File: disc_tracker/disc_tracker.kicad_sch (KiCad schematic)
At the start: 0 parts

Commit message: QFN32 added for Silabs chip. Regulator symbol added. All ICs on schematic
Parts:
- added AE1: Antenna_Chip, RF_Antenna:Pulse_W3011, symbol Device:Antenna_Chip
- added IC1: EFR32BG22C112F352GM32-CR, Package_DFN_QFN:QFN-32-1EP_4x4mm_P0.4mm_EP2.8x2.8mm, symbol RF_Bluetooth:EFR32BG22C112F352GM32-CR
- added J1: Conn_01x02_Pin, Connector_JST:JST_PH_B2B-PH-K_1x02_P2.00mm_Vertical, symbol Connector:Conn_01x02_Pin
- added U1: AP9101CK6, Package_TO_SOT_SMD:SOT-23-6, symbol Battery_Management:AP9101CK6
- added U2: TCR2LF33, Package_TO_SOT_SMD:SOT-553, symbol Regulator_Linear:TCR2LF33
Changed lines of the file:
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@@
 (kicad_sch (version 20230121) (generator eeschema)
   (paper "A4")
+  (symbol (lib_id "Battery_Management:AP9101CK6") (at 59.69 49.53 0) (unit 1)
+    (in_bom yes) (on_board yes) (dnp no) (fields_autoplaced)
+    (property "Reference" "U1" (at 61.8841 39.37 0)
+      (effects (font (size 1.27 1.27)) (justify left))
+    )
+    (property "Value" "AP9101CK6" (at 61.8841 41.91 0)
+      (effects (font (size 1.27 1.27)) (justify left))
+    )
+    (property "Footprint" "Package_TO_SOT_SMD:SOT-23-6" (at 59.69 49.53 0)
+      (effects (font (size 1.27 1.27)) hide)
+    )
+    (property "Datasheet" "https://www.diodes.com/assets/Datasheets/AP9101C.pdf" (at 59.69 48.26 0)
+      (effects (font (size 1.27 1.27)) hide)
+    )
+    (pin "1")
+    (pin "2")
+    (pin "3")
+    (pin "4")
+    (pin "5")
+    (pin "6")
+    (instances
+      (project "disc_tracker"
+        (path "/50d77920-ac47-47b2-845c-3d52e036b015"
+          (reference "U1") (unit 1)
+        )
+      )
+    )
+  )
+  (symbol (lib_id "Connector:Conn_01x02_Pin") (at 35.56 31.75 0) (unit 1)
+    (in_bom yes) (on_board yes) (dnp no) (fields_autoplaced)
+    (property "Reference" "J1" (at 36.195 26.67 0)
+      (effects (font (size 1.27 1.27)))
+    )
+    (property "Value" "Conn_01x02_Pin" (at 36.195 29.21 0)
+      (effects (font (size 1.27 1.27)))
+    )
+    (property "Footprint" "Connector_JST:JST_PH_B2B-PH-K_1x02_P2.00mm_Vertical" (at 35.56 31.75 0)
+      (effects (font (size 1.27 1.27)) hide)
+    )
+    (property "Datasheet" "~" (at 35.56 31.75 0)
+      (effects (font (size 1.27 1.27)) hide)
+    )
+    (pin "1")
+    (pin "2")
+    (instances
+      (project "disc_tracker"
+        (path "/50d77920-ac47-47b2-845c-3d52e036b015"
+          (reference "J1") (unit 1)
+        )
+      )
+    )
+  )
+  (symbol (lib_id "RF_Bluetooth:EFR32BG22C112F352GM32-CR") (at 120.65 76.2 0) (unit 1)
+    (in_bom yes) (on_board yes) (dnp no) (fields_autoplaced)
+    (property "Reference" "IC1" (at 172.72 69.2719 0)
+      (effects (font (size 1.27 1.27)))
+    )
+    (property "Value" "EFR32BG22C112F352GM32-CR" (at 172.72 71.8119 0)
+      (effects (font (size 1.27 1.27)))
+    )
+    (property "Footprint" "Package_DFN_QFN:QFN-32-1EP_4x4mm_P0.4mm_EP2.8x2.8mm" (at 157.48 158.42 0)
+      (effects (font (size 1.27 1.27)) (justify left top) hide)
+    )
+    (property "Datasheet" "https://au.mouser.com/datasheet/2/368/efr32bg22c112_datasheet-1830161.pdf" (at 157.48 258.42 0)
+      (effects (font (size 1.27 1.27)) (justify left top) hide)
+    )
+    (property "Height" "0.9" (at 157.48 458.42 0)
+      (effects (font (size 1.27 1.27)) (justify left top) hide)
+    )
+    (property "Mouser Part Number" "634-ER32BG22112352CR" (at 157.48 558.42 0)
+      (effects (font (size 1.27 1.27)) (justify left top) hide)
+    )
+    (property "Mouser Price/Stock" "https://www.mouser.co.uk/ProductDetail/Silicon-Labs/EFR32BG22C112F352GM32-CR?qs=zhx2xqPtQQy3D8%2FKsJy7oA%3D%3D" (at 157.48 658.42 0)
+      (effects (font (size 1.27 1.27)) (justify left top) hide)
+    )
+    (property "Manufacturer_Name" "Silicon Labs" (at 157.48 758.42 0)
+      (effects (font (size 1.27 1.27)) (justify left top) hide)
+    )
+    (property "Manufacturer_Part_Number" "EFR32BG22C112F352GM32-CR" (at 157.48 858.42 0)
+      (effects (font (size 1.27 1.27)) (justify left top) hide)
+    )
+    (pin "1")
+    (pin "10")
+    (pin "11")
+    (pin "12")
+    (pin "13")
+    (pin "14")
+    (pin "15")
+    (pin "16")
+    (pin "17")
+    (pin "18")
+    (pin "19")
+    (pin "2")
+    (pin "20")
+    (pin "21")
+    (pin "22")
+    (pin "23")
+    (pin "24")
+    (pin "25")
+    (pin "26")
+    (pin "27")
+    (pin "28")
+    (pin "29")
+    (pin "3")
+    (pin "30")
+    (pin "31")
+    (pin "32")
+    (pin "33")
+    (pin "4")
+    (pin "5")
+    (pin "6")
+    (pin "7")
+    (pin "8")
+    (pin "9")
+    (instances
+      (project "disc_tracker"
+        (path "/50d77920-ac47-47b2-845c-3d52e036b015"
+          (reference "IC1") (unit 1)
+        )
+      )
+    )
+  )
+  (symbol (lib_id "Device:Antenna_Chip") (at 254 33.02 0) (unit 1)
+    (in_bom yes) (on_board yes) (dnp no) (fields_autoplaced)
+    (property "Reference" "AE1" (at 259.08 29.21 0)
+      (effects (font (size 1.27 1.27)) (justify left))
+    )
+    (property "Value" "Antenna_Chip" (at 259.08 31.75 0)
+      (effects (font (size 1.27 1.27)) (justify left))
+    )
+    (property "Footprint" "RF_Antenna:Pulse_W3011" (at 251.46 28.575 0)
+      (effects (font (size 1.27 1.27)) hide)
+    )
+    (property "Datasheet" "~" (at 251.46 28.575 0)
+      (effects (font (size 1.27 1.27)) hide)
+    )
+    (pin "1")
+    (pin "2")
+    (instances
+      (project "disc_tracker"
+        (path "/50d77920-ac47-47b2-845c-3d52e036b015"
+          (reference "AE1") (unit 1)
+        )
+      )
+    )
+  )
+  (symbol (lib_id "Regulator_Linear:TCR2LF33") (at 107.95 36.83 0) (unit 1)
+    (in_bom yes) (on_board yes) (dnp no) (fields_autoplaced)
+    (property "Reference" "U2" (at 107.95 26.67 0)
+      (effects (font (size 1.27 1.27)))
+    )
+    (property "Value" "TCR2LF33" (at 107.95 29.21 0)
+      (effects (font (size 1.27 1.27)))
+    )
+    (property "Footprint" "Package_TO_SOT_SMD:SOT-553" (at 107.95 46.99 0)
+      (effects (font (size 1.27 1.27)) hide)
+    )
+    (property "Datasheet" "https://au.mouser.com/datasheet/2/408/TCR2LF10_datasheet_en_20141106-760799.pdf" (at 101.6 30.48 0)
+      (effects (font (size 1.27 1.27)) hide)
+    )
+    (pin "1")
+    (pin "2")
+    (pin "3")
+    (pin "4")
+    (pin "5")
+    (instances
+      (project "disc_tracker"
+        (path "/50d77920-ac47-47b2-845c-3d52e036b015"
+          (reference "U2") (unit 1)
+        )
+      )
+    )
+  )
   (sheet_instances
     (path "/" (page "1"))

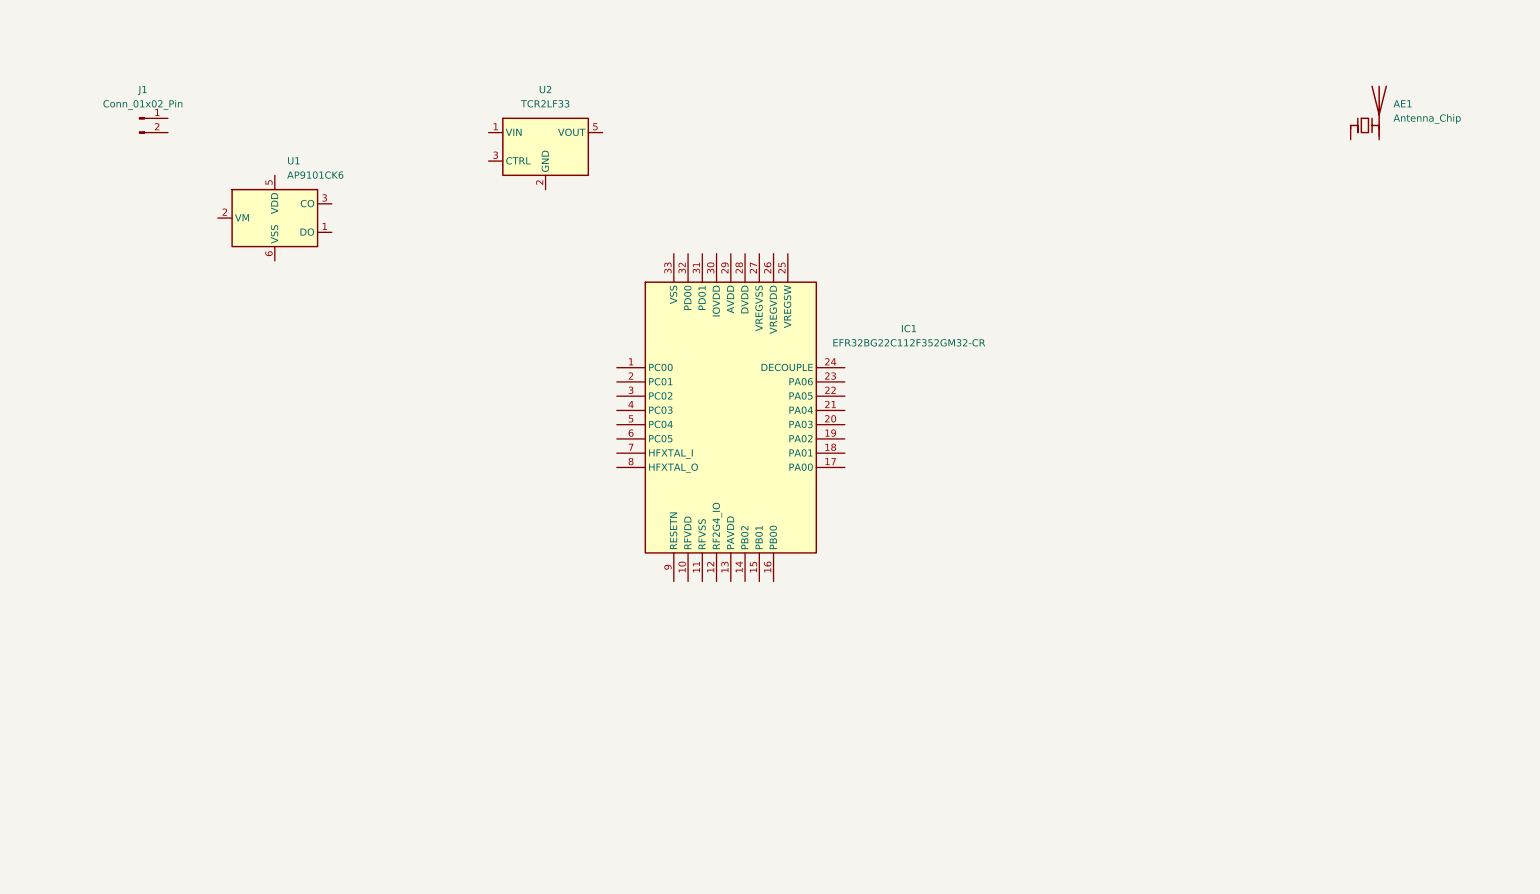
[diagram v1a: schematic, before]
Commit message: Schematic should be done. Starting component placment. Will need to go to 0201 for decoupling caps maybe
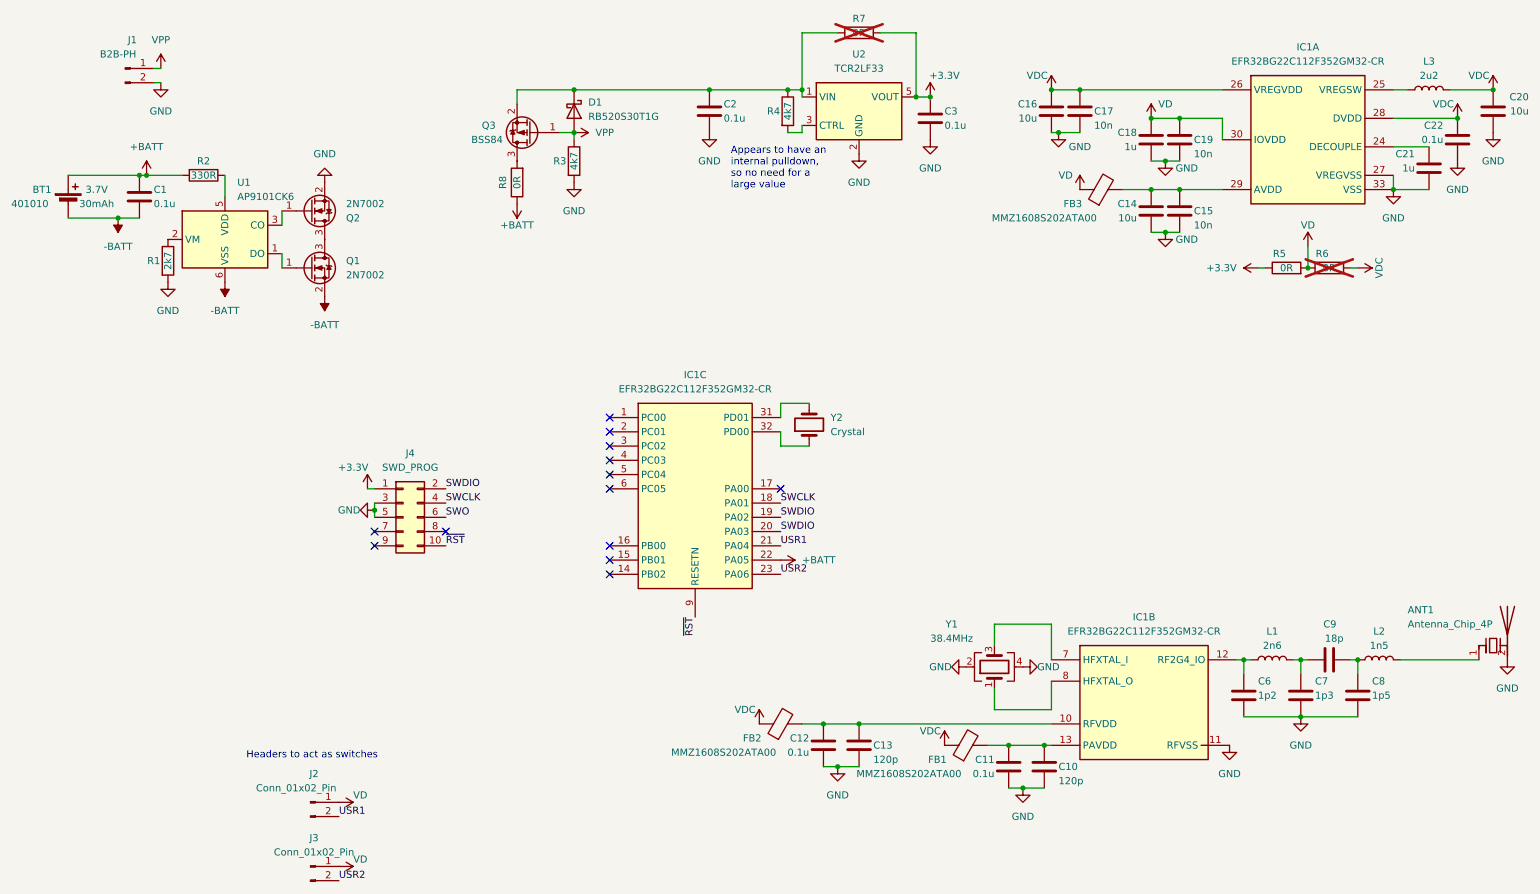
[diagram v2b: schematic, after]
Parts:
- removed AE1: Antenna_Chip, RF_Antenna:Pulse_W3011, symbol Device:Antenna_Chip
- added ANT1: Antenna_Chip_4P, RF_Antenna:2450AT18D0100E, symbol Device:Antenna_Chip_4P
- added BT1: 401010, symbol Device:Battery_Cell
- added C1, C11, C12, C2, C22, C3: 0.1u, Capacitor_SMD:C_0402_1005Metric, symbol Device:C
- added C10, C13: 120p, Capacitor_SMD:C_0402_1005Metric, symbol Device:C
- added C14, C16, C20: 10u, Capacitor_SMD:C_0603_1608Metric, symbol Device:C
- added C15, C17, C19: 10n, Capacitor_SMD:C_0402_1005Metric, symbol Device:C
- added C18, C21: 1u, Capacitor_SMD:C_0603_1608Metric, symbol Device:C
- added C6: 1p2, Capacitor_SMD:C_0402_1005Metric, symbol Device:C
- added C7: 1p3, Capacitor_SMD:C_0402_1005Metric, symbol Device:C
- added C8: 1p5, Capacitor_SMD:C_0402_1005Metric, symbol Device:C
- added C9: 18p, Capacitor_SMD:C_0402_1005Metric, symbol Device:C
- added D1: RB520S30T1G, Diode_SMD:D_SOD-523, symbol Device:D_Schottky
- added FB1, FB2, FB3: MMZ1608S202ATA00, Inductor_SMD:L_0603_1608Metric, symbol Device:FerriteBead
- added unit 3 of IC1
- added unit 2 of IC1
- added J2, J3: Conn_01x02_Pin, Connector_PinHeader_1.27mm:PinHeader_1x02_P1.27mm_Vertical, symbol Connector:Conn_01x02_Pin
- added J4: SWD_PROG, Connector_PinHeader_1.27mm:PinHeader_2x05_P1.27mm_Vertical, symbol Connector_Generic:Conn_02x05_Odd_Even
- added L1: 2n6, Inductor_SMD:L_0402_1005Metric, symbol Device:L
- added L2: 1n5, Inductor_SMD:L_0402_1005Metric, symbol Device:L
- added L3: 2u2, Inductor_SMD:L_0402_1005Metric, symbol Device:L
- added Q1, Q2: 2N7002, Package_TO_SOT_SMD:SOT-23, symbol Device:Q_NMOS_GSD
- added Q3: BSS84, Package_TO_SOT_SMD:SOT-23, symbol Device:Q_PMOS_GSD
- added R1: 2k7, Resistor_SMD:R_0402_1005Metric, symbol Device:R
- added R2: 330R, Resistor_SMD:R_0402_1005Metric, symbol Device:R
- added R3, R4: 4k7, Resistor_SMD:R_0402_1005Metric, symbol Device:R
- added R5, R6, R7, R8: 0R, Resistor_SMD:R_0402_1005Metric, symbol Device:R
- added Y1: 38.4MHz, Crystal:Crystal_SMD_2016-4Pin_2.0x1.6mm, symbol Device:Crystal_GND24
- added Y2: Crystal, Crystal:Crystal_SMD_3215-2Pin_3.2x1.5mm, symbol Device:Crystal
- J1: value Conn_01x02_Pin -> B2B-PH
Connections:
- net at U1.1 (DO): now also Q1.1 (G)
- net at U1.2 (VM): now also R1.1
- net at U1.3 (CO): now also Q2.1 (G)
- net at U1.5 (VDD): now also R2.1
- net -BATT: now reaches U1.6 (VSS)
- net -BATT: now also BT1.2 (-), C1.1, Q1.2 (S)
- net VPP: now reaches J1.1 (Pin_1)
- net VPP: now also D1.2 (A), Q3.1 (G), R3.1
- net GND: now reaches J1.2 (Pin_2)
- net GND: now also IC1.27 (VREGVSS), IC1.33 (VSS), U2.2 (GND), ANT1.2 (GND), ANT1.3 (GND), ANT1.4 (GND), C10.1, C11.1, C12.1, C13.1, C14.1, C15.1, C16.1, C17.1, C18.1, C19.1, C2.1, C20.1, C21.1, C22.1, C3.1, C6.1, C7.1, C8.1, IC1.11 (RFVSS), J4.3 (Pin_3), J4.5 (Pin_5), Q2.2 (S), R1.2, R3.2, Y1.2, Y1.4
- net at IC1.24 (DECOUPLE): now also C21.2
- net at IC1.25 (VREGSW): now also L3.1
- net VDC: now reaches IC1.26 (VREGVDD)
- net VDC: now also IC1.28 (DVDD), C16.2, C17.2, C20.2, C22.2, FB1.1, FB2.1, L3.2, R6.2
- net at IC1.29 (AVDD): now also C14.2, C15.2, FB3.2
- net VD: now reaches IC1.30 (IOVDD)
- net VD: now also C18.2, C19.2, FB3.1, J2.1 (Pin_1), J3.1 (Pin_1), R5.2, R6.1
- net at U2.1 (VIN): now also C2.2, D1.1 (K), Q3.2 (S), R4.1, R7.1
- net at U2.3 (CTRL): now also R4.2
- net +3.3V: now reaches U2.5 (VOUT)
- net +3.3V: now also C3.2, J4.1 (Pin_1), R5.1, R7.2
- new net: Q1.3 (D), Q2.3 (D)
- new net: C12.2, C13.2, FB2.2, IC1.10 (RFVDD)
- new net: C10.2, C11.2, FB1.2, IC1.13 (PAVDD)
- new net: IC1.31 (PD01), Y2.2
- new net: IC1.32 (PD00), Y2.1
- new net: C6.2, IC1.12 (RF2G4_IO), L1.1
- new net: C7.2, C9.2, L1.2
- new net: C8.2, C9.1, L2.1
- new net: Q3.3 (D), R8.2
- new net: IC1.7 (HFXTAL_I), Y1.3
- new net: IC1.8 (HFXTAL_O), Y1.1
- new net: ANT1.1 (FEED), L2.2
- new net +BATT: BT1.1 (+), C1.2, IC1.22 (PA05), R2.2, R8.1
- new net SWCLK: IC1.18 (PA01), J4.4 (Pin_4)
- new net SWDIO: IC1.19 (PA02), IC1.20 (PA03), J4.2 (Pin_2)
- new net SWO: J4.6 (Pin_6)
- new net USR1: IC1.21 (PA04), J2.2 (Pin_2)
- new net USR2: IC1.23 (PA06), J3.2 (Pin_2)
- new net ~{RST}: IC1.9 (RESETN), J4.10 (Pin_10)
- no-connect marks 0 -> 13
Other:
- note added: "Appears to have an internal pulldown, so no need for a large value"
- note added: "Headers to act as switches"
- moved on the sheet: U1, U2
